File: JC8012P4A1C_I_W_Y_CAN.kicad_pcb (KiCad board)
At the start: 6 copper layers, 66 x 54 mm, 39 parts, among them J1 610110249121, J2 68711414522, J3 653104131822, Q1 Si4948BEY, U1 TLE9250VSJ, U2 171030601

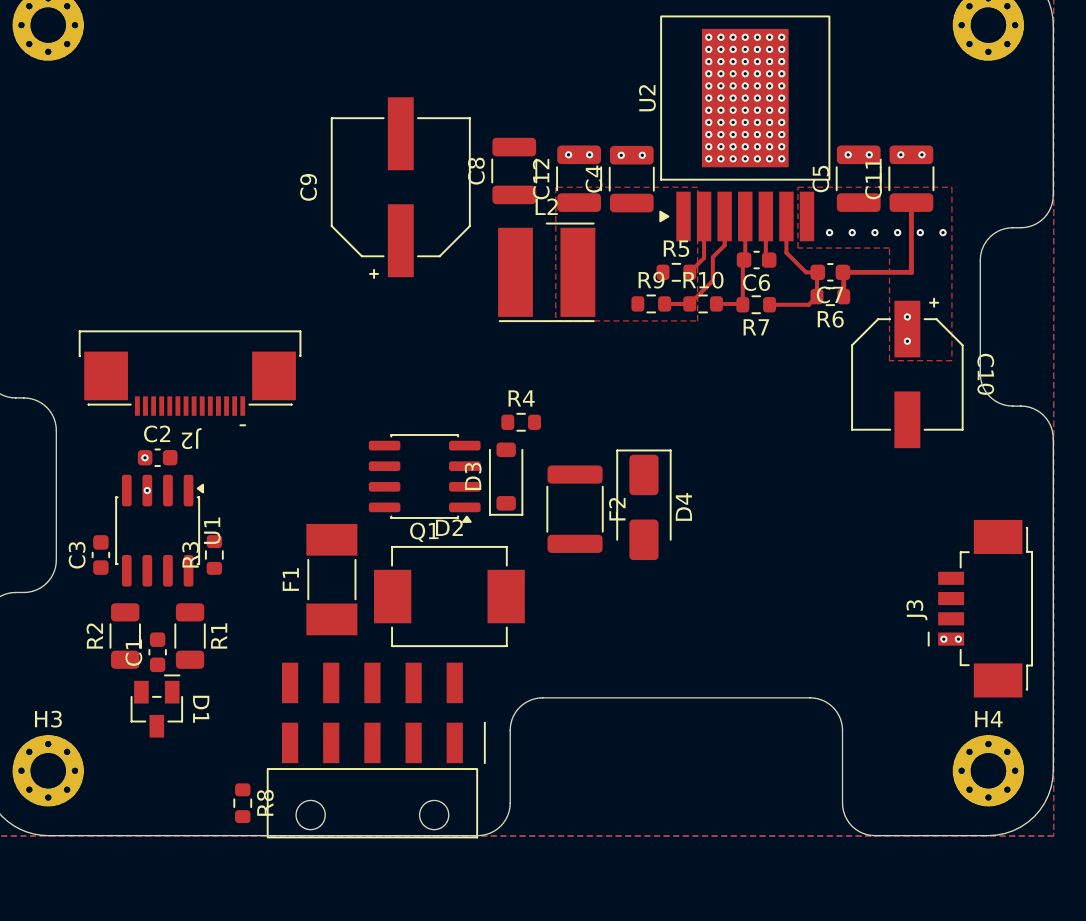
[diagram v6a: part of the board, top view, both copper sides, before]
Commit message: GND vias in every SMD GND pad
Outside the buck converter there was no GND via at all; the GND pads
only reached the inner GND planes through the F.Cu pour and the
mounting holes (25-50 mm). Add 27 vias 0.45/0.2: one per small pad,
two per large pad (C8, C9, C10, D2, J1, J2 Z1/Z2, J3 MP1/MP2).
J2 pins 1/2 are too narrow (0.3 mm) and use the Z1/Z2 vias.
DRC: unconnected items 35 -> 0.

Co-Authored-By: Claude Opus 5.5 <noreply@anthropic.com>
Claude-Session: https://claude.ai/code/session_014h8cGi8SRWthYdGFH1Qgzz
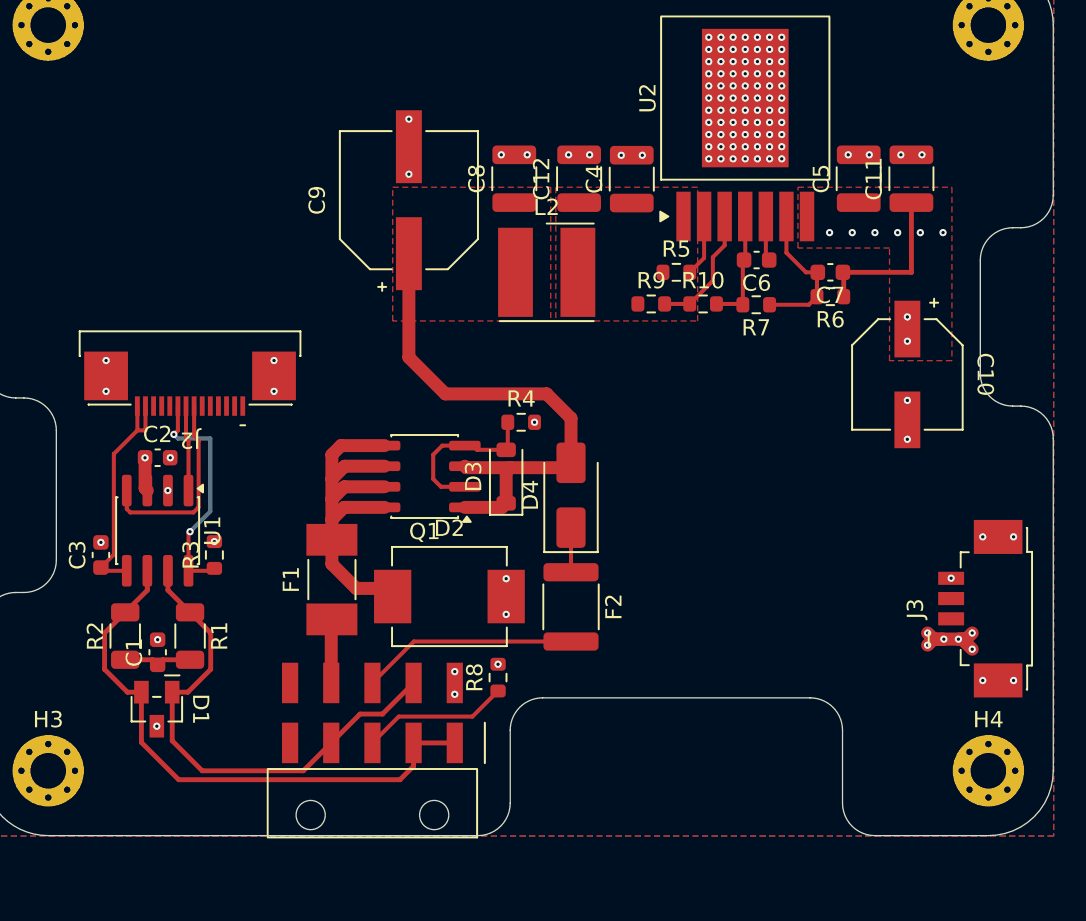
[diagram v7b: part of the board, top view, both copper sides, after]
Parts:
- moved R8 17.6 mm to (131.8, 144.2), turned to 90 degrees
- moved F2 6.03 mm to (136.2, 139.9)
- moved D4 4.56 mm to (136.2, 133.0), turned to 90 degrees
- moved C9 0.94 mm to (126.2, 114.8)
- moved C8 0.47 mm to (132.8, 113.5)
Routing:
- net /CAN_L: track 0.00 -> 35.2 mm
- net /Versorgung/VIN_PROT: track 0.00 -> 32.4 mm
- net /CAN_H: track 0.00 -> 31.0 mm
- net /Versorgung/ECU_PWR: track 0.00 -> 25.5 mm
- net /CAN_NEN: track 0.00 -> 14.6 mm, vias 0 -> 2
- net /+3V3: track 0.00 -> 14.6 mm
- net TBC_PWR_OUT: track 0.00 -> 13.3 mm
- net /CAN_RXD: track 0.00 -> 12.1 mm
- net /Versorgung/PFET_G: track 0.00 -> 10.2 mm
- net /TBC_GND: track 0.00 -> 9.08 mm
- net +5V: track 10.0 -> 16.6 mm, vias 12 -> 15
- net /CAN_TXD: track 0.00 -> 5.28 mm
- net /CAN_SPLIT: track 0.00 -> 4.26 mm
- net ECU_PWR_IN: track 0.00 -> 3.94 mm
- net Net-(D4-K): track 0.00 -> 2.75 mm
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- added copper zone on F.Cu, net /Versorgung/VIN_PROT

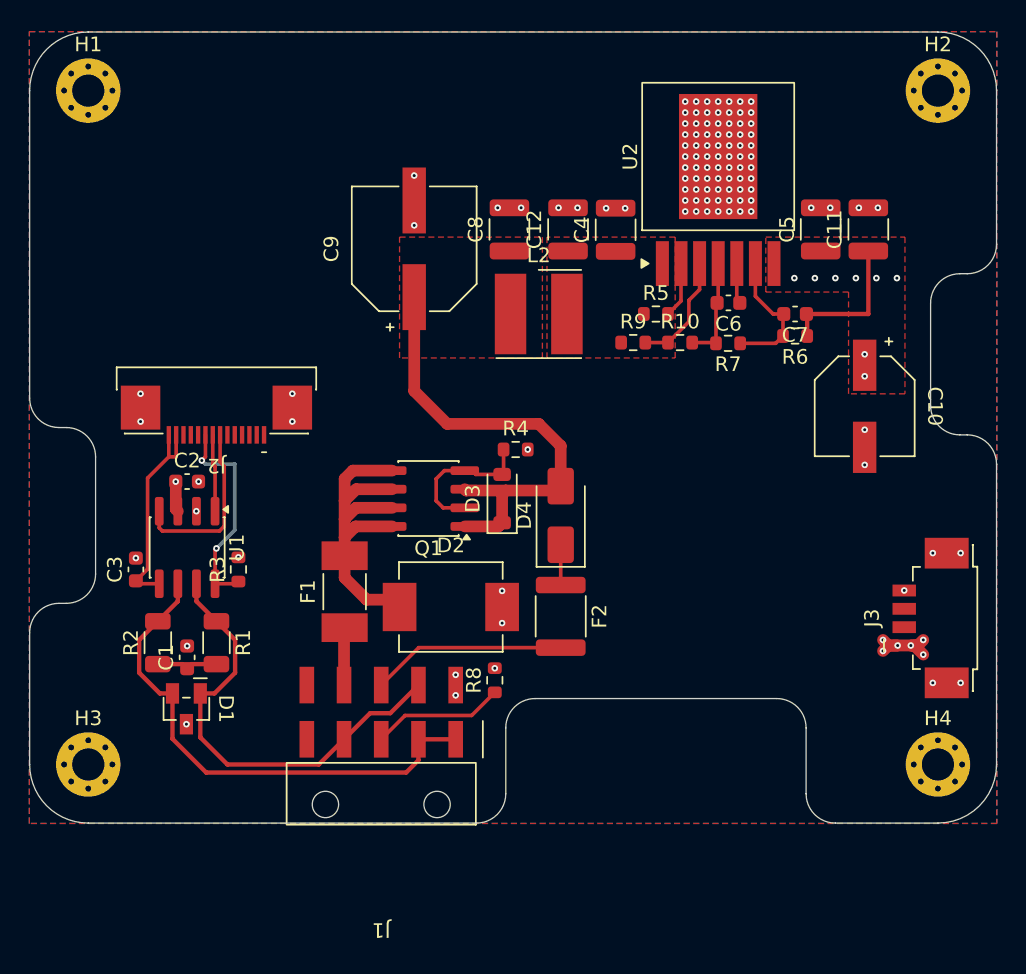
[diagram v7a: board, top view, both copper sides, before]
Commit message: GND stitching, GND plane on In3, silkscreen cleanup
- 155 GND stitching vias 0.45/0.2 on a 4 mm grid, only inside the GND
  pour, none in the mounting holes or in the VIN_PROT/VIN_BUCK pours
- In3 was empty: GND pour on In3 (copper balance against the +5V plane
  on In2, one more GND plane)
- Reference designators placed off pads, vias, courtyards and other
  silkscreen; J1 reference was outside the board. D2 and C1 use 0.8 mm
  text (0.15 mm stroke) for lack of space
- J1 footprint: silkscreen rectangle replaced by a U-frame open towards
  the board edge (the housing is flush with the edge)
DRC: 0 violations, 0 unconnected. ERC: 0.

Co-Authored-By: Claude Opus 5.5 <noreply@anthropic.com>
Claude-Session: https://claude.ai/code/session_014h8cGi8SRWthYdGFH1Qgzz
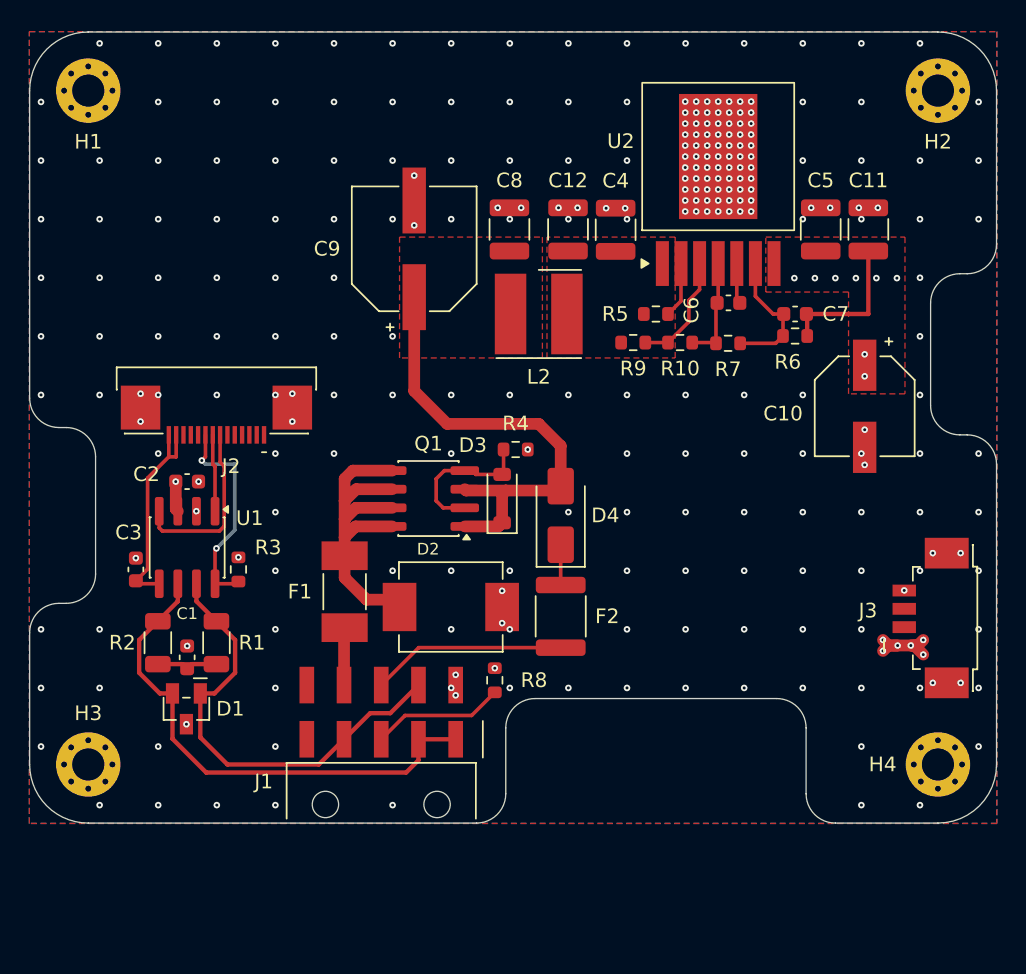
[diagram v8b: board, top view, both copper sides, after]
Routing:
- net GND: vias 112 -> 267
- added copper zone on In3.Cu, net GND
